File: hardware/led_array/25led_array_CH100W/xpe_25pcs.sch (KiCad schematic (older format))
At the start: 26 parts, among them J1 Conn_01x10

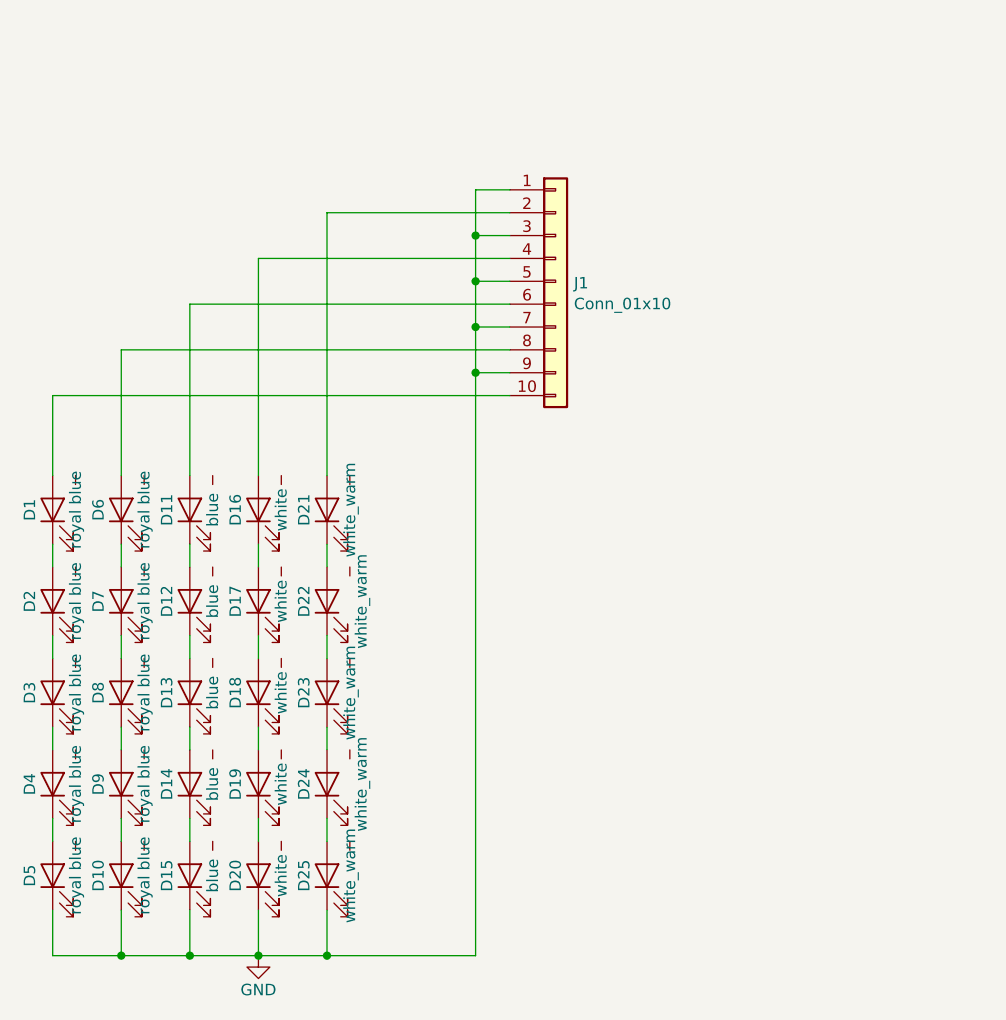
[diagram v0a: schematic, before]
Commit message: controller schematic draft finished
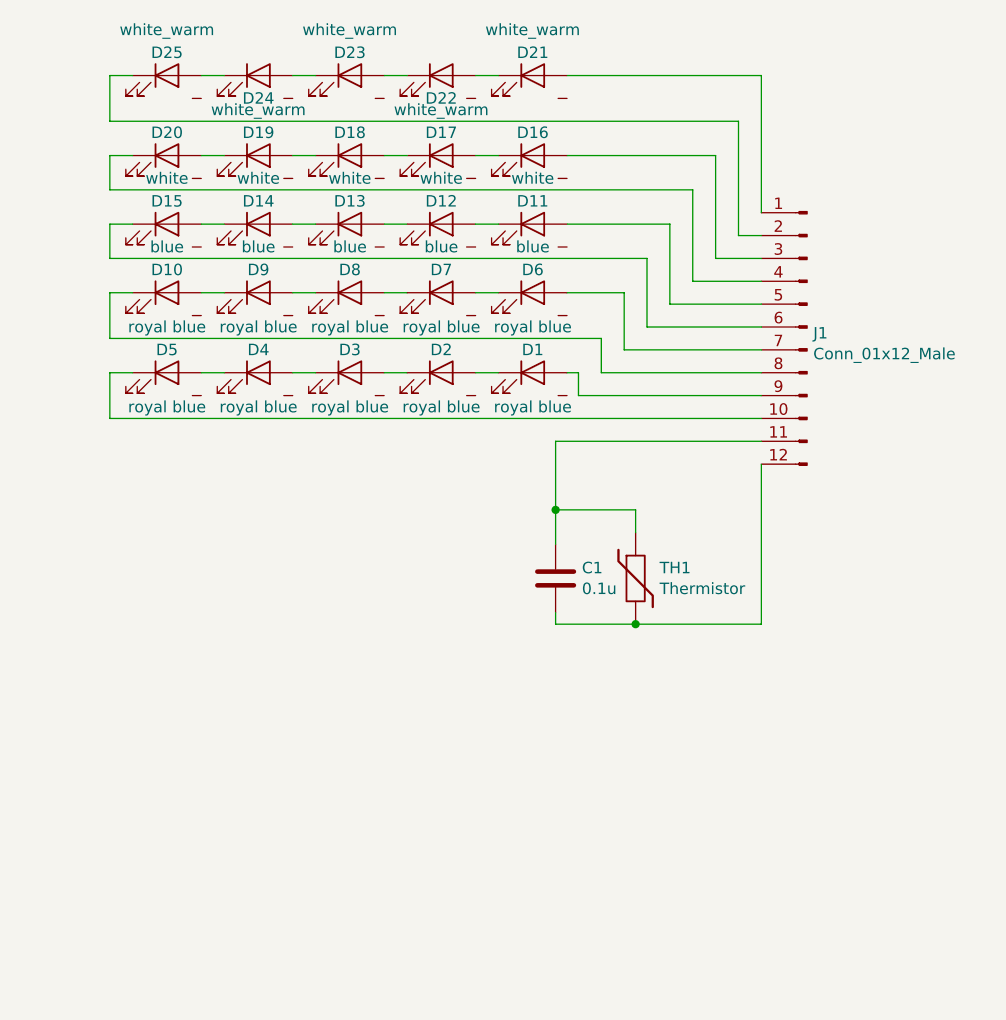
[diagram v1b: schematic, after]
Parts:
- removed J1: Conn_01x10, led:header_10_smd, symbol Connector_Generic:Conn_01x10
- added C1: 0.1u, Capacitor_SMD:C_0603_1608Metric_Pad1.05x0.95mm_HandSolder, symbol Device:C
- added J1: Conn_01x12_Male, led:header_12_smd, symbol Connector:Conn_01x12_Male
- added TH1: Thermistor, Capacitor_SMD:C_0603_1608Metric_Pad1.05x0.95mm_HandSolder, symbol Device:Thermistor
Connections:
- net at D1.2 (A): now also J1.9 (Pin_9)
- net at D6.2 (A): now also J1.7 (Pin_7)
- net at D21.2 (A): now also J1.1 (Pin_1)
- net at D16.2 (A): now also J1.3 (Pin_3)
- net at D11.2 (A): now also J1.5 (Pin_5)
- removed net GND: D10.1 (K), D15.1 (K), D20.1 (K), D25.1 (K), D5.1 (K)
- new net: D5.1 (K), J1.10 (Pin_10)
- new net: D10.1 (K), J1.8 (Pin_8)
- new net: D15.1 (K), J1.6 (Pin_6)
- new net: D20.1 (K), J1.4 (Pin_4)
- new net: D25.1 (K), J1.2 (Pin_2)
- new net: C1.1, J1.11 (Pin_11), TH1.1
- new net: C1.2, J1.12 (Pin_12), TH1.2
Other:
- moved on the sheet: D1, D10, D11, D12, D13, D14, D15, D16, D17, D18, D19, D2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

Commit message: open source hardware fix
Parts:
- TH1: value Thermistor -> NTCS0603E3103
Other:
- note added: "Copyright Alexander Khoroshko 2018.\nThis documentation describes Open Hardware and is licensed under the CERN OHL v. 1.2. \nYou may redistribute and modify this documentation under the terms of the CERN OHL v.1.2. \nThis documentation is distributed WITHOUT ANY EXPRESS OR IMPLIED WARRANTY, INCLUDING \nOF MERCHANTABILITY, SATISFACTORY QUALITY AND FITNESS FOR A PARTICULAR PURPOSE. \nPlease see the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"
- note added: "Reef open hardware light (ROHL) 25 LED module"
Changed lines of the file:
@@
 U 1 1 5C0B8E85
 P 6750 3750
-F 0 "TH1" H 6855 3796 50  0000 L CNN
-F 1 "Thermistor" H 6855 3705 50  0000 L CNN
+F 0 "TH1" H 6850 3750 50  0000 L CNN
+F 1 "NTCS0603E3103" H 6855 3705 50  0001 L CNN
 F 2 "Capacitor_SMD:C_0603_1608Metric_Pad1.05x0.95mm_HandSolder" H 6750 3750 50  0001 C CNN
 F 3 "~" H 6750 3750 50  0001 C CNN
@@
 Wire Wire Line
 	6600 2700 6600 2850
+Text Notes 7050 7100 0    50   ~ 0
+Copyright Alexander Khoroshko 2018.\nThis   documentation   describes   Open   Hardware   and   is   licensed   under   the CERN OHL v. 1.2. \nYou may redistribute and modify this documentation under the terms of the CERN OHL v.1.2. \nThis documentation is distributed WITHOUT   ANY   EXPRESS   OR   IMPLIED   WARRANTY,   INCLUDING \nOF MERCHANTABILITY,   SATISFACTORY   QUALITY   AND   FITNESS   FOR   A PARTICULAR   PURPOSE.   \nPlease   see   the   CERN   OHL   v.1.2  for   applicable conditions.
+Text Notes 7350 7500 0    50   ~ 0
+Reef open hardware light (ROHL) 25 LED module
 $EndSCHEMATC

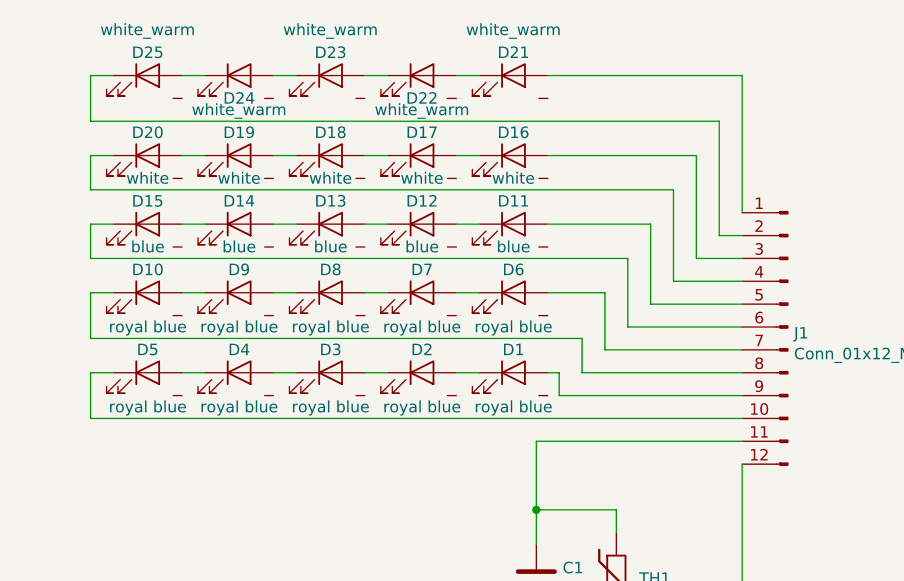
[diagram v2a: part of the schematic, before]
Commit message: led array rework for fr4 board
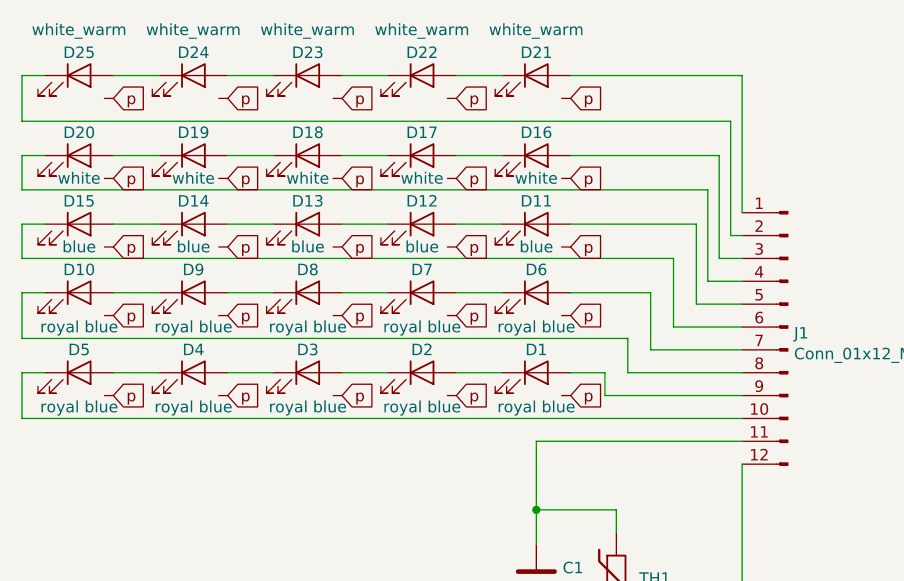
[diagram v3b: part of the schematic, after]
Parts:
- D1, D10, D11, D12, D13, D14, D15, D16, D17, D18, D19, D2, D20, D21, D22, D23, D24, D25, D3, D4, D5, D6, D7, D8, D9: footprint led:LED_Cree-XP-E -> led:LED_Cree-XP-E_vias
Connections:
- net p: now reaches D5.3 (pad)
- net p: now also D1.3 (pad), D10.3 (pad), D11.3 (pad), D12.3 (pad), D13.3 (pad), D14.3 (pad), D15.3 (pad), D16.3 (pad), D17.3 (pad), D18.3 (pad), D19.3 (pad), D2.3 (pad), D20.3 (pad), D21.3 (pad), D22.3 (pad), D23.3 (pad), D24.3 (pad), D25.3 (pad), D3.3 (pad), D4.3 (pad), D6.3 (pad), D7.3 (pad), D8.3 (pad), D9.3 (pad)
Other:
- moved on the sheet: D1, D10, D11, D13, D14, D15, D16, D18, D19, D20, D21, D23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
